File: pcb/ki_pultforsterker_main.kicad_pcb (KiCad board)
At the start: 2 copper layers, 150 x 100 mm, 145 parts, among them J1 24V IN, J10 LED-RINGER, J2 SPK L, J3 SPK R, J4 AUX, J5 RPi 40-pin, J6 5V -> PI, J7 KNAPPER, J8 ENCODER, J9 OLED, K1 G6K-2P-Y 5VDC, Q1 AO3400A, Q2 AO3400A, Q3 AO3400A, Q4 AO3400A, Q5 AO3400A, Q6 AO3400A, U1 TPS54560BDDA, U2 AMS1117-3.3, U3 ICL7660, U4 PCM5102APW, U5 PGA2311UA, U6 TPA3116D2DAD

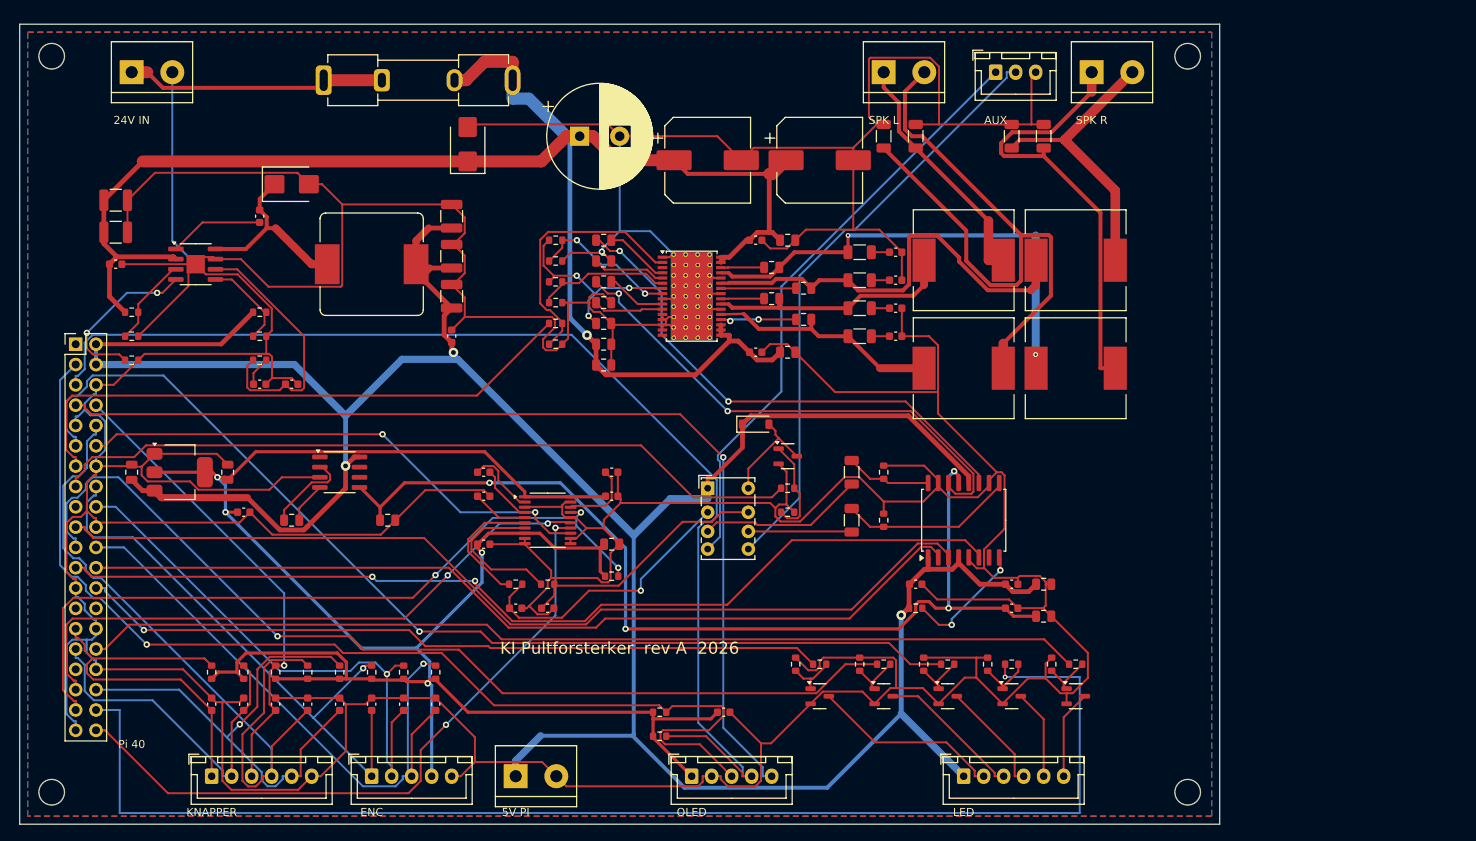
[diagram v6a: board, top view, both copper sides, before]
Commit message: pcb rev B: rutet på nytt med hodetelefonforsterker (TPA6132A2, J23) – alle nett koblet, DRC uten klarings-/hullfeil
- export.py: fjerner ubrukte låste hjelpespor/vias på tekstnivå, mikrosegmenter filtreres ved SES-import
- produksjon/: gerber, drill, BOM, CPL, DRC-rapport regenerert

Co-Authored-By: Claude Fable 5.1 <noreply@anthropic.com>
Claude-Session: https://claude.ai/code/session_01FaJKmYinw8SWRobKXBRYpt
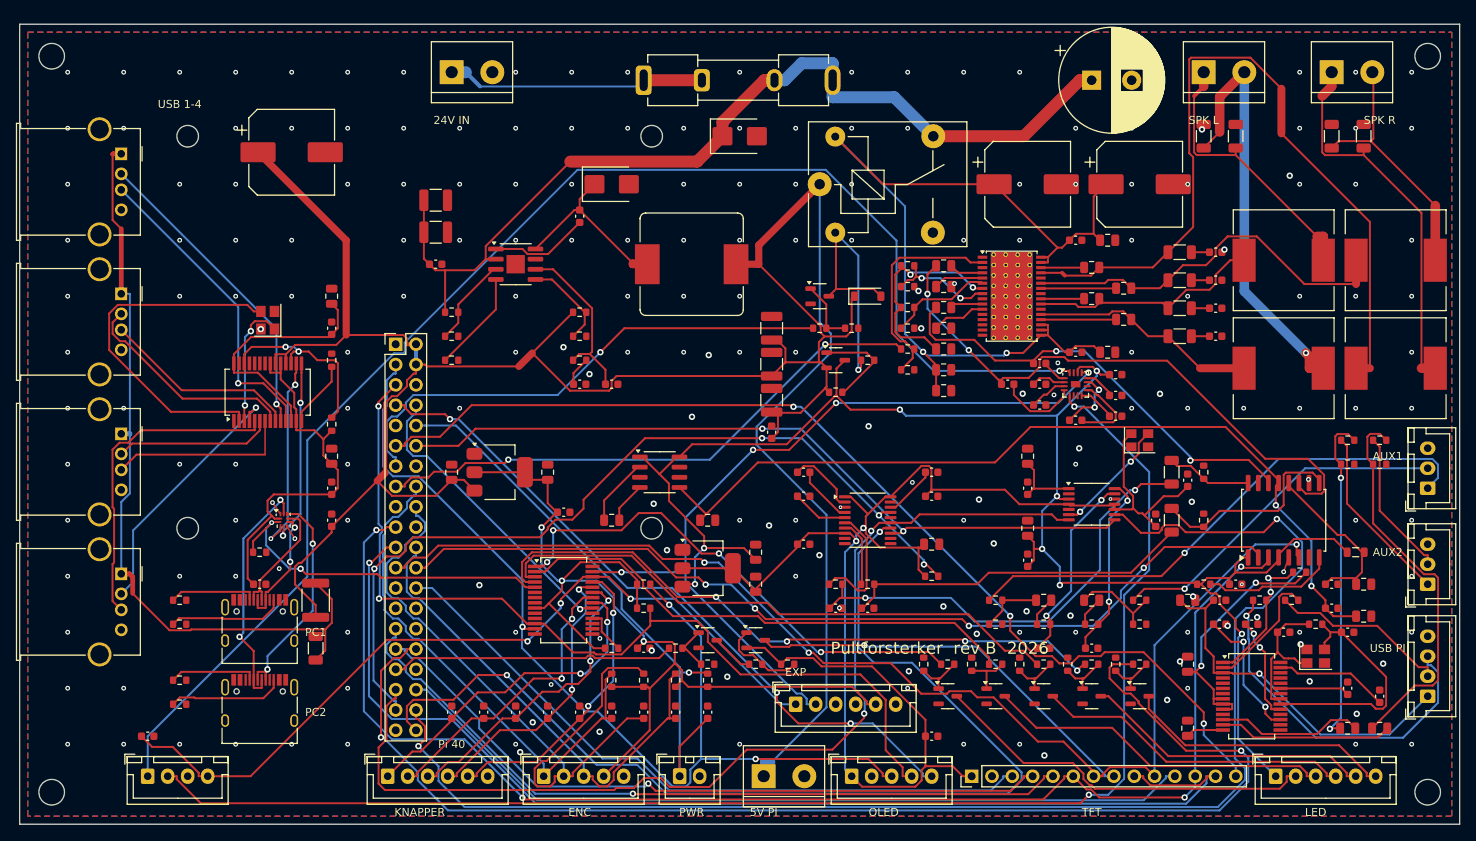
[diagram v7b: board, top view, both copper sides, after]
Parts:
- removed D3: 1N4148W, D_SOD-123
- removed Q1: AO3400A, SOT-23-3
- removed R10: 100, R_0603_1608Metric
- removed R11: 100k, R_0603_1608Metric
- removed R35, R36, R37, R38, R39: 10k, R_0603_1608Metric
- added C100: 2.2u, C_0603_1608Metric, F.Cu at (137.0, 43.8)
- added C101: 2.2u, C_0603_1608Metric, F.Cu at (137.0, 46.4)
- added C102: 1u, C_0603_1608Metric, F.Cu at (137.0, 49.0)
- added C103: 1u, C_0603_1608Metric, F.Cu at (132.0, 49.5)
- added C104: 1u, C_0603_1608Metric, F.Cu at (127.5, 42.4)
- added C105: 1u, C_0603_1608Metric, F.Cu at (127.5, 45.0)
- added C106: 1u, C_0603_1608Metric, F.Cu at (127.5, 47.6)
- added C107: 1u, C_0603_1608Metric, F.Cu at (123.5, 45.0)
- added C108: 100n, C_0603_1608Metric, F.Cu at (16.0, 89.0)
- added C66: 10u, C_0805_2012Metric, F.Cu at (39.0, 54.0)
- added C67: 10u, C_0805_2012Metric, F.Cu at (39.0, 34.0)
- added C68: 100n, C_0603_1608Metric, F.Cu at (39.0, 62.0)
- added C69: 100n, C_0603_1608Metric, F.Cu at (39.0, 38.0)
- added C70: 100n, C_0603_1608Metric, F.Cu at (30.0, 70.0)
- added C71: 10u, C_1206_3216Metric, F.Cu at (37.0, 78.0)
- added C72: 220u/35V, CP_Elec_10x10.5, F.Cu at (34.0, 16.0)
- added C73: 100n, C_0603_1608Metric, F.Cu at (39.0, 58.0)
- added C74: 100n, C_0603_1608Metric, F.Cu at (78.0, 78.0)
- added C75: 10u, C_0805_2012Metric, F.Cu at (92.0, 66.0)
- added C76: 10u, C_0805_2012Metric, F.Cu at (92.0, 70.0)
- added C77: 100n, C_0603_1608Metric, F.Cu at (146.0, 57.0)
- added C78: 10u, C_0805_2012Metric, F.Cu at (126.0, 54.0)
- added C79: 100n, C_0603_1608Metric, F.Cu at (126.0, 58.0)
- added C80: 10u, C_0805_2012Metric, F.Cu at (126.0, 63.0)
- added C81: 100n, C_0603_1608Metric, F.Cu at (126.0, 67.0)
- added C82: 100n, C_0603_1608Metric, F.Cu at (142.0, 62.0)
- added C83: 4.7u, C_0805_2012Metric, F.Cu at (128.0, 72.0)
- added C84: 4.7u, C_0805_2012Metric, F.Cu at (134.0, 72.0)
- added C85: 1n, C_0603_1608Metric, F.Cu at (128.0, 78.0)
- added C86: 1n, C_0603_1608Metric, F.Cu at (134.0, 78.0)
- added C87: 20p, C_0603_1608Metric, F.Cu at (158.0, 76.0)
- added C88: 20p, C_0603_1608Metric, F.Cu at (166.0, 76.0)
- added C89: 10u, C_0805_2012Metric, F.Cu at (146.0, 80.0)
- added C90: 10u, C_0805_2012Metric, F.Cu at (146.0, 88.0)
- added C91: 1u, C_0603_1608Metric, F.Cu at (150.0, 75.0)
- added C92: 1u, C_0603_1608Metric, F.Cu at (154.0, 75.0)
- added C93: 1u, C_0603_1608Metric, F.Cu at (166.0, 83.0)
- added C94: 1u, C_0603_1608Metric, F.Cu at (170.0, 84.0)
- added C95: 10u, C_0805_2012Metric, F.Cu at (146.0, 72.0)
- added C96: 100n, C_0603_1608Metric, F.Cu at (150.0, 72.0)
- added C97: 4.7u, C_0805_2012Metric, F.Cu at (166.0, 88.0)
- added C98: 4.7u, C_0805_2012Metric, F.Cu at (170.0, 88.0)
- added C99: 100n, C_0603_1608Metric, F.Cu at (114.0, 89.0)
- added D4: 1N4148W, D_SOD-123, F.Cu at (106.0, 34.0)
- added F2: 2A PTC, Fuse_1812_4532Metric, F.Cu at (37.0, 72.0)
- added FB1: 600R@100MHz, L_0805_2012Metric, F.Cu at (167.0, 66.0)
- added H5: M2.5, MountingHole_2.7mm_M2.5, F.Cu at (21.0, 14.0)
- added H6: M2.5, MountingHole_2.7mm_M2.5, F.Cu at (79.0, 14.0)
- added H7: M2.5, MountingHole_2.7mm_M2.5, F.Cu at (21.0, 63.0)
- added H8: M2.5, MountingHole_2.7mm_M2.5, F.Cu at (79.0, 63.0)
- added J11: PC1, USB_C_Receptacle_HRO_TYPE-C-31-M-12, F.Cu at (30.0, 76.0)
- added J12: PC2, USB_C_Receptacle_HRO_TYPE-C-31-M-12, F.Cu at (30.0, 86.0)
- added J13: TFT, PinHeader_1x14_P2.54mm_Vertical, F.Cu at (119.0, 94.0)
- added J15: USB1, USB_A_Molex_67643_Horizontal, F.Cu at (12.7, 16.2)
- added J16: USB2, USB_A_Molex_67643_Horizontal, F.Cu at (12.7, 33.7)
- added J17: USB3, USB_A_Molex_67643_Horizontal, F.Cu at (12.7, 51.2)
- added J18: USB4, USB_A_Molex_67643_Horizontal, F.Cu at (12.7, 68.7)
- added J19: USB PI, JST_XH_B4B-XH-A_1x04_P2.50mm_Vertical, F.Cu at (176.0, 84.0)
- added J20: AUX2, JST_XH_B3B-XH-A_1x03_P2.50mm_Vertical, F.Cu at (176.0, 70.0)
- added J21: PWR BAK, JST_XH_B2B-XH-A_1x02_P2.50mm_Vertical, F.Cu at (82.5, 94.0)
- added J22: EXP, JST_XH_B6B-XH-A_1x06_P2.50mm_Vertical, F.Cu at (97.0, 85.0)
- added J23: HODETLF, JST_XH_B4B-XH-A_1x04_P2.50mm_Vertical, F.Cu at (16.0, 94.0)
- added Q10: AO3401A, SOT-23-3, F.Cu at (92.0, 77.0)
- added Q7: AO3400A, SOT-23-3, F.Cu at (100.0, 34.0)
- added Q8: AO3401A, SOT-23-3, F.Cu at (102.0, 42.0)
- added Q9: AO3400A, SOT-23-3, F.Cu at (86.0, 77.0)
- added R45: 10k, R_0603_1608Metric, F.Cu at (86.0, 82.0)
- added R46: 10k, R_0603_1608Metric, F.Cu at (39.0, 50.0)
- added R47: 100k, R_0603_1608Metric, F.Cu at (30.0, 66.0)
- added R48: 5.1k, R_0603_1608Metric, F.Cu at (20.0, 72.0)
- added R49: 5.1k, R_0603_1608Metric, F.Cu at (20.0, 75.0)
- added R50: 5.1k, R_0603_1608Metric, F.Cu at (20.0, 82.0)
- added R51: 5.1k, R_0603_1608Metric, F.Cu at (20.0, 85.0)
- added R52: 100, R_0603_1608Metric, F.Cu at (100.0, 38.0)
- added R53: 100k, R_0603_1608Metric, F.Cu at (104.0, 38.0)
- added R54: 10k, R_0603_1608Metric, F.Cu at (106.0, 42.0)
- added R55: 100k, R_0603_1608Metric, F.Cu at (102.0, 46.0)
- added R56: 10k, R_0603_1608Metric, F.Cu at (74.0, 78.0)
- added R57: 10k, R_0603_1608Metric, F.Cu at (122.0, 72.0)
- added R58: 10k, R_0603_1608Metric, F.Cu at (122.0, 75.0)
- added R59: 10k, R_0603_1608Metric, F.Cu at (140.0, 72.0)
- added R60: 10k, R_0603_1608Metric, F.Cu at (140.0, 75.0)
- added R61: 1k, R_0603_1608Metric, F.Cu at (128.0, 75.0)
- added R62: 1k, R_0603_1608Metric, F.Cu at (134.0, 75.0)
- added R63: 1M, R_0603_1608Metric, F.Cu at (162.0, 75.0)
- added R64: 22, R_0603_1608Metric, F.Cu at (155.0, 72.0)
- added R65: 22, R_0603_1608Metric, F.Cu at (159.0, 72.0)
- added R66: 1.5k, R_0603_1608Metric, F.Cu at (160.0, 68.5)
- added R67: 10k, R_0603_1608Metric, F.Cu at (166.0, 52.0)
- added R68: 4.7k, R_0603_1608Metric, F.Cu at (166.0, 55.0)
- added R69: 10k, R_0603_1608Metric, F.Cu at (170.0, 52.0)
- added R70: 4.7k, R_0603_1608Metric, F.Cu at (170.0, 55.0)
- added R71: 100, R_0603_1608Metric, F.Cu at (82.0, 78.0)
- added R72: 100k, R_0603_1608Metric, F.Cu at (86.0, 80.0)
- added R73: 10k, R_0603_1608Metric, F.Cu at (92.0, 80.0)
- added R74: 100k, R_0603_1608Metric, F.Cu at (96.0, 80.0)
- added R75: 2.7k, R_0603_1608Metric, F.Cu at (39.0, 42.0)
- added U10: PCM1808PW, TSSOP-14_4.4x5mm_P0.65mm, F.Cu at (134.0, 60.0)
- added U11: PCM2900CDB, SSOP-28_5.3x10.2mm_P0.65mm, F.Cu at (154.0, 84.0)
- added U12: MCP23017-E/SS, SSOP-28_5.3x10.2mm_P0.65mm, F.Cu at (68.0, 72.0)
- added U13: TPA6132A2RTER, Texas_RTE_WQFN-16-1EP_3x3mm_P0.5mm_EP1.2x0.8mm, F.Cu at (132.0, 45.0)
- added U7: FE1.1s, SSOP-28_5.3x10.2mm_P0.65mm, F.Cu at (31.0, 46.0)
- added U8: TS3USB221, UQFN-10_1.4x1.8mm_P0.4mm, F.Cu at (33.0, 62.0)
- added U9: AMS1117-3.3, SOT-223-3_TabPin2, F.Cu at (86.0, 68.0)
- added X1: 12.288MHz, Oscillator_SMD_Abracon_ASE-4Pin_3.2x2.5mm, F.Cu at (140.0, 52.0)
- added Y1: 12MHz, Crystal_SMD_3225-4Pin_3.2x2.5mm, F.Cu at (31.0, 37.0)
- added Y2: 12MHz, Crystal_SMD_3225-4Pin_3.2x2.5mm, F.Cu at (162.0, 79.0)
- J4: value AUX -> AUX1
- K1: value G6K-2P-Y 5VDC -> SRD-05VDC-SL-C; footprint Relay_DPDT_Omron_G6K-2P-Y -> Relay_SPDT_SANYOU_SRD_Series_Form_C
- U3: value ICL7660 -> LM2662MX
- moved J4 75.0 mm to (176.0, 58.0), turned to 90 degrees
- moved C1 64.4 mm to (134.0, 7.00)
- moved R15 44.1 mm to (111.0, 30.2)
- moved R17 44.1 mm to (111.0, 35.4)
- moved R18 44.1 mm to (111.0, 38.0)
- moved R19 44.1 mm to (111.0, 40.6)
- moved R20 44.1 mm to (111.0, 43.2)
- moved R16 44.1 mm to (111.0, 32.8)
- moved C42 42.6 mm to (115.5, 43.2)
- moved C43 42.6 mm to (115.5, 45.8)
- moved C44 42.6 mm to (115.5, 40.6)
- moved C45 42.6 mm to (115.5, 35.4)
- moved C46 42.6 mm to (115.5, 38.0)
- moved C47 42.6 mm to (115.5, 30.2)
- moved C48 42.6 mm to (115.5, 32.8)
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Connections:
- C20 pad 1: 3V3 -> 3V3_SW
- C21 pad 1: 3V3 -> 3V3_SW
- C22 pad 1: 3V3 -> 3V3_SW
- C25 pad 1: SEL_L -> DAC_L_F
- C26 pad 1: SEL_R -> DAC_R_F
- C27 pad 1: 5V -> 5V_SW
- C28 pad 1: 5V -> 5VA
- C30 pad 1: 5V -> 5VA
- C36 pad 1: VIN24 -> 24V_AMP
- C37 pad 1: VIN24 -> 24V_AMP
- C38 pad 1: VIN24 -> 24V_AMP
- C39 pad 1: VIN24 -> 24V_AMP
- C40 pad 1: VIN24 -> 24V_AMP
- C41 pad 1: VIN24 -> 24V_AMP
- C42 pad 1: VIN24 -> 24V_AMP
- C43 pad 1: VIN24 -> 24V_AMP
- C65 pad 1: 3V3 -> BTN_BAK
- J10 pad 1: 5V -> 5V_SW
- J4 pad 1: AUX_L -> AUX1_L
- J4 pad 2: AUX_R -> AUX1_R
- J5 pad 10: BTN_USB -> BTN_BAK
- J5 pad 11: LED_AUX_G -> TOUCH_IRQ
- J5 pad 13: AMP_SD_G -> PWR_G
- J5 pad 15: RLY_G -> AMP_SD_G
- J5 pad 21: LED_BT_G -> SPI_MISO
- J5 pad 26: LED_AIR_G -> TFT_CS
- J5 pad 29: BTN_AIR -> TFT_DC
- J5 pad 31: BTN_BT -> TFT_RST
- J5 pad 33: (no net) -> TFT_BL_G
- J5 pad 36: BTN_PWR -> TOUCH_CS
- J5 pad 38: LED_USB_G -> I2S_ADC
- J5 pad 8: BTN_AUX -> MCP_INT
- J9 pad 1: 3V3 -> 3V3_SW
- K1 pad 2: DAC_L_F -> RLY_LOW
- K1 pad 3: SEL_L -> (no net)
- K1 pad 4: AUX_L -> VIN24
- K1 pad 5: AUX_R -> 24V_AMP
- R14 pad 1: 5V -> 5V_SW
- R7 pad 1: 3V3 -> 3V3_SW
- U3 pad 1: (no net) -> 5V_SW
- U3 pad 8: 5V -> 5V_SW
- U4 pad 1: 3V3 -> 3V3_SW
- U4 pad 20: 3V3 -> 3V3_SW
- U4 pad 8: 3V3 -> 3V3_SW
- U5 pad 1: 5V -> 5V_SW
- U5 pad 12: 5V -> 5VA
- U5 pad 4: 5V -> 5V_SW
- U6 pad 17: VIN24 -> 24V_AMP
- U6 pad 18: VIN24 -> 24V_AMP
- U6 pad 19: VIN24 -> 24V_AMP
- U6 pad 31: VIN24 -> 24V_AMP
- U6 pad 32: VIN24 -> 24V_AMP
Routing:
- net GND: track 1091.3 -> 5.48 mm, vias 1 -> 205
- net 5V_SW: track 0.00 -> 202.7 mm, vias 0 -> 8
- net 3V3_SW: track 0.00 -> 190.2 mm, vias 0 -> 2
- net HP_OUTL: track 0.00 -> 177.6 mm, vias 0 -> 1
- net I2S_ADC: track 0.00 -> 176.5 mm, vias 0 -> 2
- net HP_OUTR: track 0.00 -> 176.4 mm, vias 0 -> 2
- net SPI_MISO: track 0.00 -> 145.5 mm, vias 0 -> 1
- net TOUCH_IRQ: track 0.00 -> 131.1 mm, vias 0 -> 3
- net 24V_AMP: track 0.00 -> 115.7 mm, vias 0 -> 2
- net 3V3: track 243.5 -> 128.3 mm, vias 4 -> 3
- net TOUCH_CS: track 0.00 -> 102.0 mm
- net EXP_A5: track 0.00 -> 101.8 mm, vias 0 -> 3
- net EXP_A6: track 0.00 -> 101.5 mm, vias 0 -> 4
- net 5V_USB: track 0.00 -> 97.5 mm
- net TFT_DC: track 0.00 -> 95.8 mm, vias 0 -> 1
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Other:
- board size 150 x 100 mm -> 180 x 100 mm
- board text added: "AUX1"
- board text added: "AUX2"
- board text added: "EXP"
- board text added: "PC1"
- board text added: "PC2"
- board text added: "PWR"
- board text added: "Pultforsterker rev B 2026"
- board text added: "TFT"
- board text added: "USB 1-4"
- board text added: "USB PI"
- board text removed: "AUX"
- board text removed: "KI Pultforsterker rev A 2026"
